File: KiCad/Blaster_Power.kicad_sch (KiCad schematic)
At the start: 17 parts, among them SW1 SW_SPST, U1 LT1172

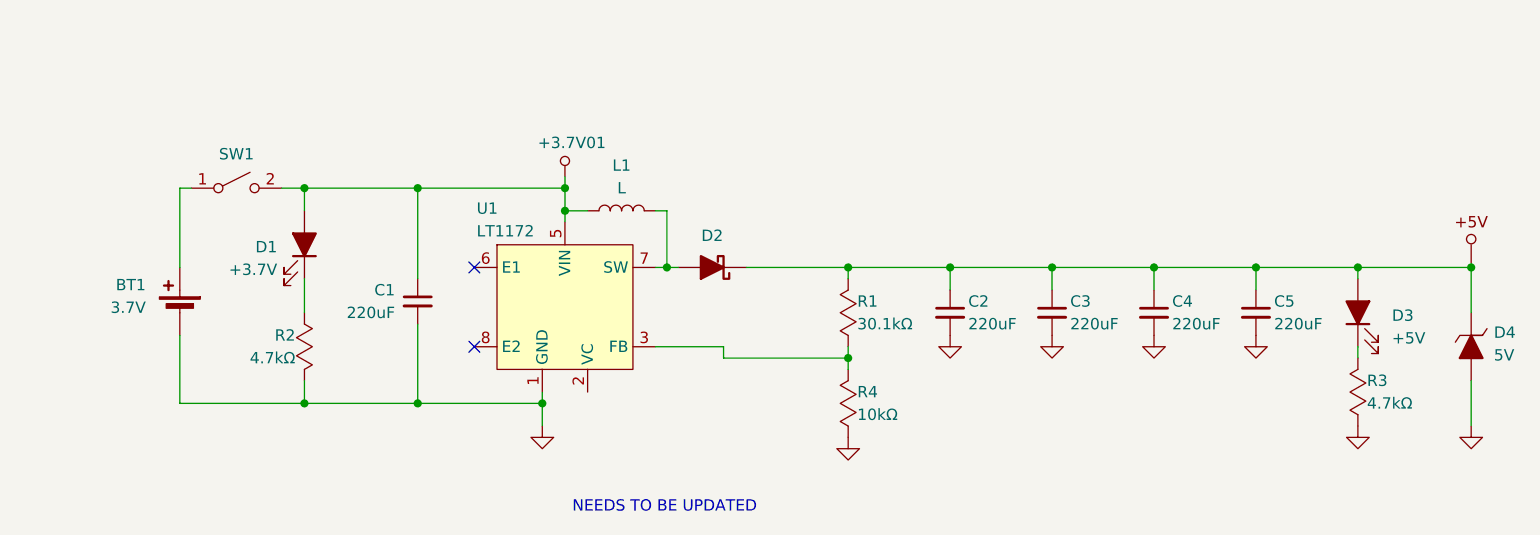
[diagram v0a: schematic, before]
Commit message: Updated blaster schematic
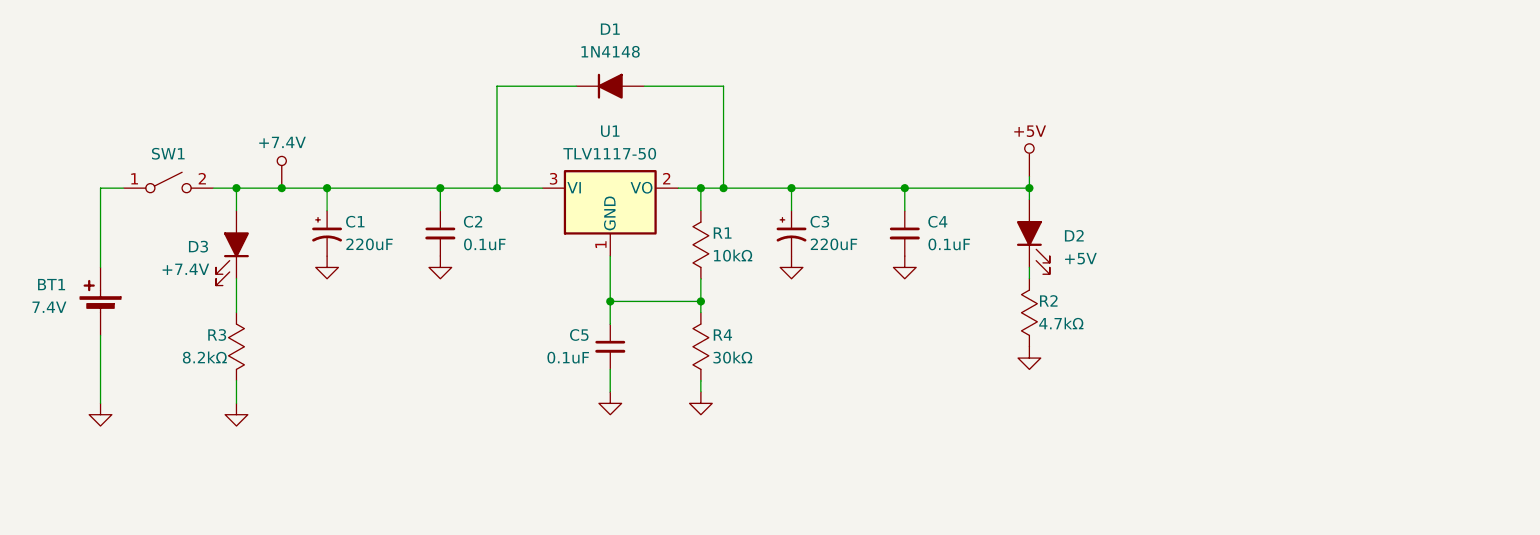
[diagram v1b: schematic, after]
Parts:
- removed C1, C3: 220uF, symbol Device:C_Small
- removed D2: D_Schottky_Filled, symbol Device:D_Schottky_Filled
- removed D4: 5V, symbol Libraries:D_Zener_Filled
- removed L1: L, symbol Device:L
- removed U1: LT1172, symbol Libraries:LT1172
- added C2: 0.1uF, symbol Device:C_Small
- added C3: 220uF, symbol Device:C_Polarized_Small_US
- added D1: 1N4148, symbol Device:D_Filled
- added U1: TLV1117-50, symbol Regulator_Linear:TLV1117-50
- BT1: value 3.7V -> 7.4V
- C1: renamed from C2; symbol Device:C_Small -> Device:C_Polarized_Small_US
- C4, C5: value 220uF -> 0.1uF
- D3: renamed from D1; value +3.7V -> +7.4V
- R1: value 30.1kΩ -> 10kΩ
- R3: renamed from R2; value 4.7kΩ -> 8.2kΩ
- R4: value 10kΩ -> 30kΩ
- renumbered D3 to D2, R3 to R2
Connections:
- net +5V: now also C3.1, D1.2 (A), U1.2 (VO); no longer C1.1, C5.1
- net GND: now also C2.2, C3.2
- net at D3.2 (A), SW1.2 (B): now also C1.1, C2.1, D1.1 (K), U1.3 (VI)
- net at R1.1, R4.2: now also C5.1, U1.1 (GND)
- no-connect marks 2 -> 0
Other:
- note removed: "NEEDS TO BE UPDATED"
- moved on the sheet: BT1, D2, D3, R2, R3, SW1

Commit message: Finalized schematics
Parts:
- removed C5: 0.1uF, symbol Device:C_Small
- removed R1: 10kΩ, symbol Libraries:R_Custom
- removed R4: 30kΩ, symbol Libraries:R_Custom
- added J2: Inputs Test Points, Connector_PinHeader_2.54mm:PinHeader_1x05_P2.54mm_Vertical, symbol Libraries:Header_1x5
- added J3: Power & Output Test Points, Connector_PinHeader_2.54mm:PinHeader_1x04_P2.54mm_Vertical, symbol Libraries:Header_1x4
- BT1: footprint (none) -> AlexWheelockFootprintLibrary:Project_Battery_Connector
- C1, C3: footprint (none) -> AlexWheelockFootprintLibrary:Project_16V_220uF_Capacitor
- C2, C4: footprint (none) -> Capacitor_SMD:C_0805_2012Metric_Pad1.18x1.45mm_HandSolder
- D1: footprint (none) -> Diode_SMD:D_0805_2012Metric_Pad1.15x1.40mm_HandSolder
- D2, D3: footprint (none) -> LED_SMD:LED_0805_2012Metric_Pad1.15x1.40mm_HandSolder
- R2, R3: footprint (none) -> Resistor_SMD:R_0805_2012Metric_Pad1.20x1.40mm_HandSolder
- SW1: value SW_SPST -> Power; footprint (none) -> AlexWheelockFootprintLibrary:Project_Locking_Output_Header
- U1: footprint (none) -> Package_TO_SOT_SMD:SOT-223-3_TabPin2
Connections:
- net +5V: now also J3.2
- net GND: now also U1.1 (GND)
- new net +7.4V: J3.1
- new net Burst: J2.4
- new net Fire: J2.1
- new net Frequency Select: J2.2
- new net Full-Auto: J2.3
- new net Laser/PWM: J3.3
- new net Semi-Auto: J2.5
- new net Solenoid: J3.4
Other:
- moved on the sheet: BT1

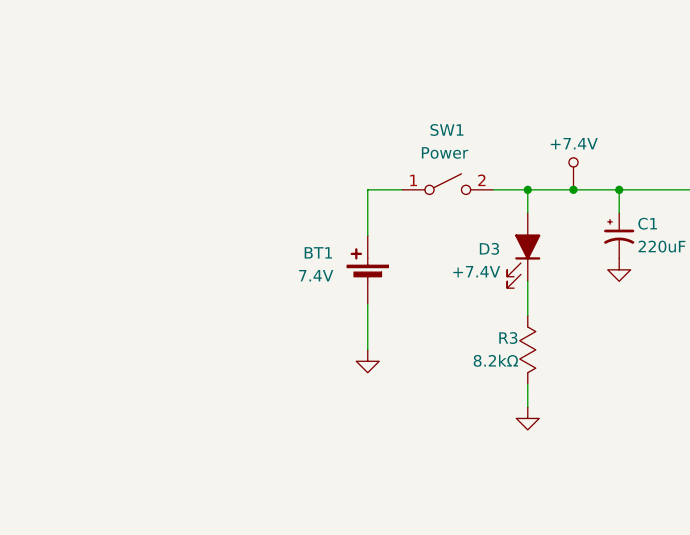
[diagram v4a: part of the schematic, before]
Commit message: recovered some lost parts of the schematic, still needs a bit of work to get back
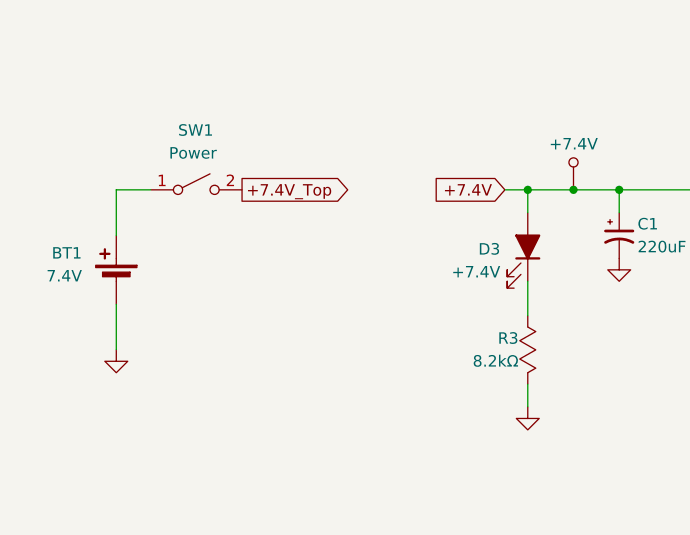
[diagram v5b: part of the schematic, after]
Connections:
- net +7.4V: now also C1.1, C2.1, D1.1 (K), D3.2 (A), U1.3 (VI)
- new net +7.4V_Top: SW1.2 (B)
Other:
- moved on the sheet: BT1, SW1
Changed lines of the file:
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@@
+	(wire
+		(pts
+			(xy 95.25 82.55) (xy 97.79 82.55)
+		)
+		(stroke
+			(width 0)
+			(type default)
+		)
+	)
 	(wire
 		(pts
@@
 	(wire
 		(pts
-			(xy 80.01 82.55) (xy 83.82 82.55)
+			(xy 52.07 82.55) (xy 55.88 82.55)
 		)
 		(stroke
@@
 	(wire
 		(pts
-			(xy 80.01 100.33) (xy 80.01 95.25)
+			(xy 52.07 100.33) (xy 52.07 95.25)
 		)
 		(stroke
@@
 	(wire
 		(pts
-			(xy 93.98 82.55) (xy 97.79 82.55)
-		)
-		(stroke
-			(width 0)
-			(type default)
-		)
-	)
-	(wire
-		(pts
 			(xy 82.55 172.72) (xy 85.09 172.72)
 		)
@@
 	(wire
 		(pts
-			(xy 80.01 87.63) (xy 80.01 82.55)
+			(xy 52.07 87.63) (xy 52.07 82.55)
 		)
 		(stroke
@@
 			(width 0)
 			(type default)
+		)
+	)
+	(global_label "+7.4V_Top"
+		(shape output)
+		(at 66.04 82.55 0)
+		(fields_autoplaced yes)
+		(effects
+			(font
+				(size 1.27 1.27)
+			)
+			(justify left)
+		)
+		(property "Intersheetrefs" "${INTERSHEET_REFS}"
+			(at 78.9432 82.55 0)
+			(effects
+				(font
+					(size 1.27 1.27)
+				)
+				(justify left)
+				(hide yes)
+			)
 		)
 	)
@@
 		)
 	)
+	(global_label "+7.4V"
+		(shape input)
+		(at 95.25 82.55 180)
+		(fields_autoplaced yes)
+		(effects
+			(font
+				(size 1.27 1.27)
+			)
+			(justify right)
+		)
+		(property "Intersheetrefs" "${INTERSHEET_REFS}"
+			(at 86.58 82.55 0)
+			(effects
+				(font
+					(size 1.27 1.27)
+				)
+				(justify right)
+				(hide yes)
+			)
+		)
+	)
 	(symbol
 		(lib_id "Switch:SW_SPST")
-		(at 88.9 82.55 0)
+		(at 60.96 82.55 0)
 		(unit 1)
 		(exclude_from_sim no)
@@
 		(dnp no)
 		(property "Reference" "SW1"
-			(at 86.868 75.946 0)
+			(at 58.928 75.946 0)
 			(effects
 				(font
@@
 		)
 		(property "Value" "Power"
-			(at 85.852 78.486 0)
+			(at 57.912 78.486 0)
 			(effects
 				(font
@@
 		)
 		(property "Footprint" "AlexWheelockFootprintLibrary:Project_Locking_Output_Header"
-			(at 88.9 82.55 0)
+			(at 60.96 82.55 0)
 			(effects
 				(font
@@
 		)
 		(property "Datasheet" "~"
-			(at 88.9 82.55 0)
+			(at 60.96 82.55 0)
 			(effects
 				(font
@@
 		)
 		(property "Description" "Single Pole Single Throw (SPST) switch"
-			(at 88.9 82.55 0)
+			(at 60.96 82.55 0)
 			(effects
 				(font
@@
 	(symbol
 		(lib_id "Device:Battery_Cell")
-		(at 80.01 92.71 0)
+		(at 52.07 92.71 0)
 		(mirror y)
 		(unit 1)
@@
 		(dnp no)
 		(property "Reference" "BT1"
-			(at 76.2 89.5984 0)
+			(at 48.26 89.5984 0)
 			(effects
 				(font
@@
 		)
 		(property "Value" "7.4V"
-			(at 76.2 92.1384 0)
+			(at 48.26 92.1384 0)
 			(effects
 				(font
@@
 		)
 		(property "Footprint" "AlexWheelockFootprintLibrary:Project_Battery_Connector"
-			(at 80.01 91.186 90)
+			(at 52.07 91.186 90)
 			(effects
 				(font
@@
 		)
 		(property "Datasheet" "~"
-			(at 80.01 91.186 90)
+			(at 52.07 91.186 90)
 			(effects
 				(font
@@
 		)
 		(property "Description" "Single-cell battery"
-			(at 80.01 92.71 0)
+			(at 52.07 92.71 0)
 			(effects
 				(font
@@
 	(symbol
 		(lib_id "power:GND")
-		(at 80.01 100.33 0)
+		(at 52.07 100.33 0)
 		(unit 1)
 		(exclude_from_sim no)
@@
 		(fields_autoplaced yes)
 		(property "Reference" "#PWR06"
-			(at 80.01 106.68 0)
+			(at 52.07 106.68 0)
 			(effects
 				(font
@@
 		)
 		(property "Value" "GND"
-			(at 80.01 105.41 0)
+			(at 52.07 105.41 0)
 			(effects
 				(font
@@
 		)
 		(property "Footprint" ""
-			(at 80.01 100.33 0)
+			(at 52.07 100.33 0)
 			(effects
 				(font
@@
 		)
 		(property "Datasheet" ""
-			(at 80.01 100.33 0)
+			(at 52.07 100.33 0)
 			(effects
 				(font
@@
 		)
 		(property "Description" "Power symbol creates a global label with name \"GND\" , ground"
-			(at 80.01 100.33 0)
-			(effects
-				(font
+			(at 52.07 100.33 0)
+			(effects
+				(font

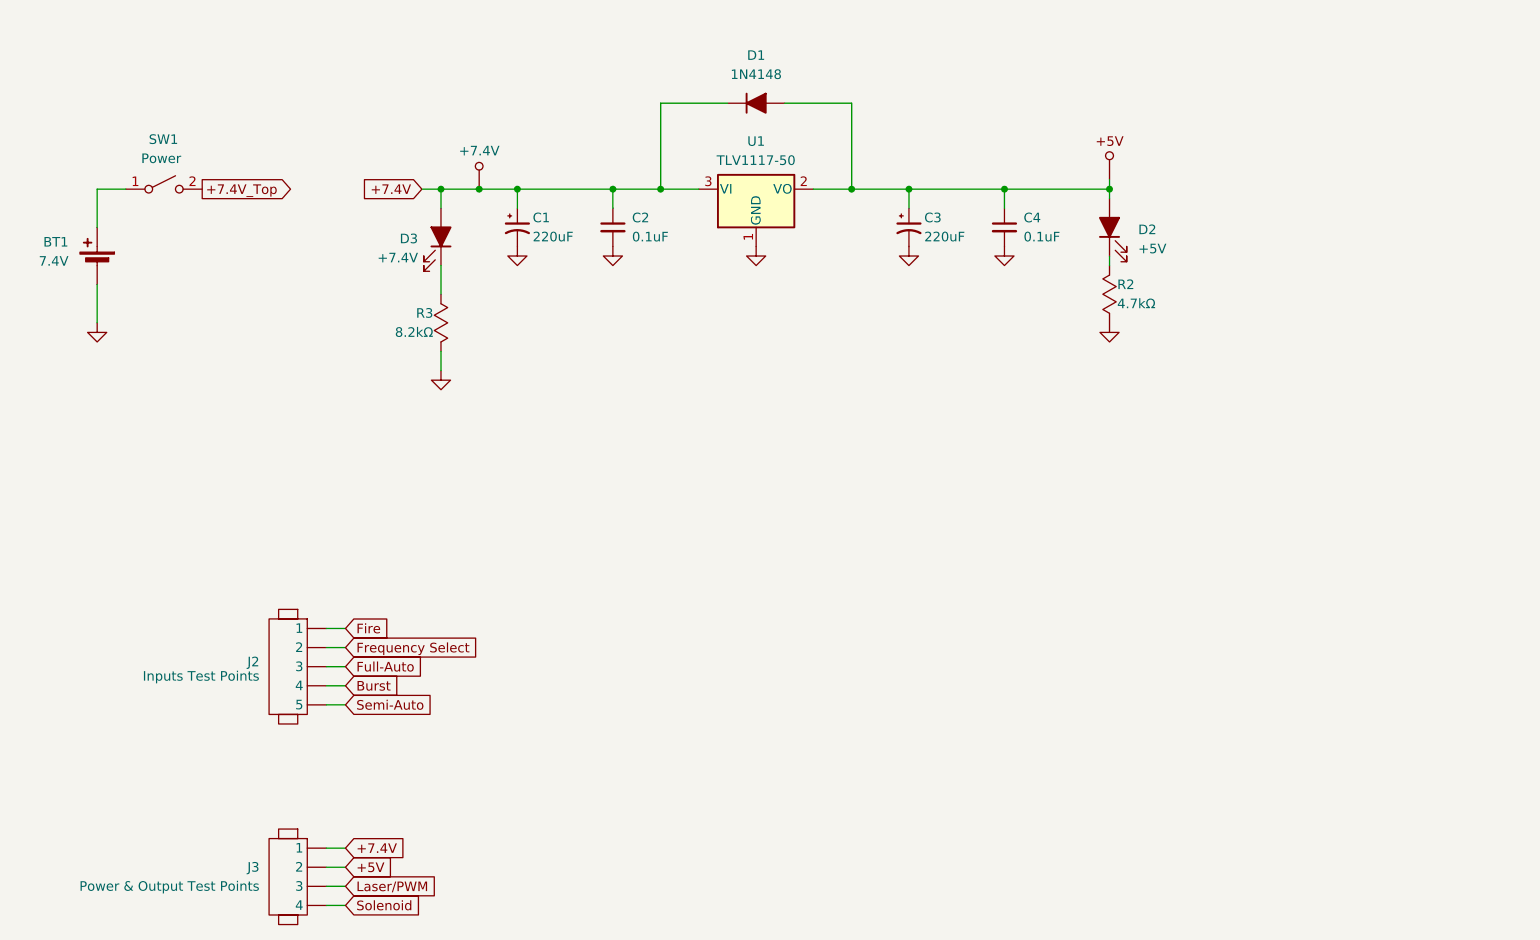
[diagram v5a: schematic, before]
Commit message: fixed the schematics, and got the new components added into the PCB, need to rerun a lot of traces.
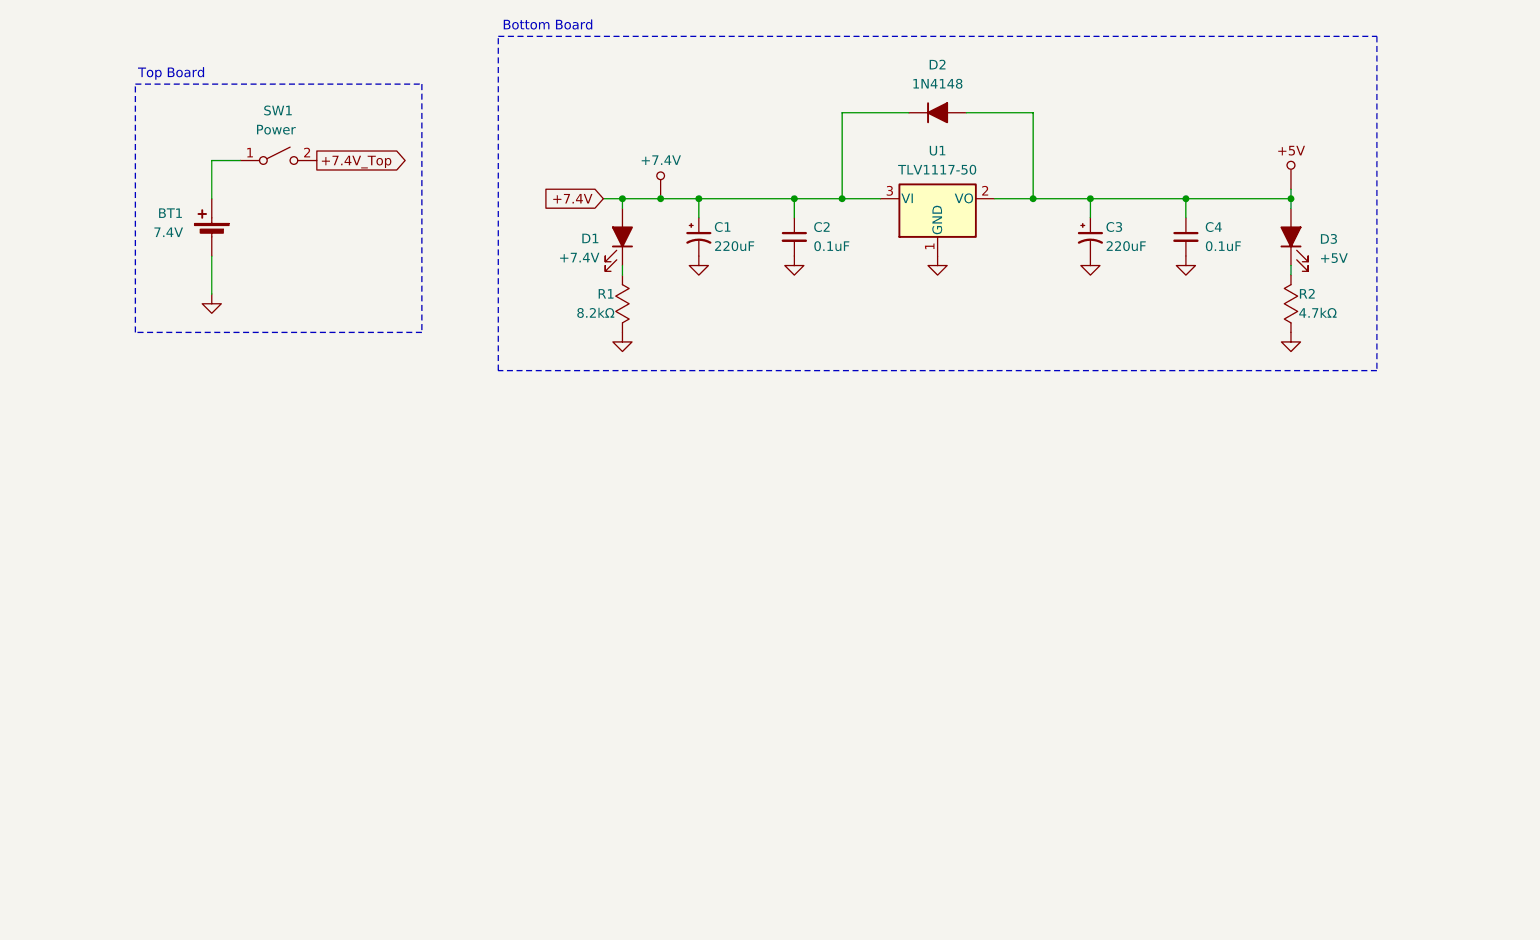
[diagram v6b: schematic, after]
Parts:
- removed J2: Inputs Test Points, Connector_PinHeader_2.54mm:PinHeader_1x05_P2.54mm_Vertical, symbol Libraries:Header_1x5
- removed J3: Power & Output Test Points, Connector_PinHeader_2.54mm:PinHeader_1x04_P2.54mm_Vertical, symbol Libraries:Header_1x4
- renumbered D3 to D1, D1 to D2, D2 to D3, R3 to R1
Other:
- note added: "Bottom Board"
- note added: "Top Board"
- moved on the sheet: BT1, C1, C2, C3, C4, D1, D2, D3, R1, R2, SW1, U1

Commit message: PCB nearly done for the blaster
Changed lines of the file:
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@@
+	)
+	(junction
+		(at 210.82 81.28)
+		(diameter 0)
+		(color 0 0 0 0)
 	)
 	(junction
@@
 	(wire
 		(pts
+			(xy 210.82 81.28) (xy 213.36 81.28)
+		)
+		(stroke
+			(width 0)
+			(type default)
+		)
+	)
+	(wire
+		(pts
 			(xy 151.13 83.82) (xy 156.21 83.82)
 		)
@@
 	(wire
 		(pts
-			(xy 210.82 83.82) (xy 210.82 82.55)
+			(xy 210.82 83.82) (xy 210.82 81.28)
 		)
 		(stroke
@@
 		(pts
 			(xy 171.45 83.82) (xy 176.53 83.82)
+		)
+		(stroke
+			(width 0)
+			(type default)
+		)
+	)
+	(wire
+		(pts
+			(xy 210.82 81.28) (xy 210.82 80.01)
 		)
 		(stroke
@@
 		)
 	)
+	(global_label "+5V"
+		(shape output)
+		(at 213.36 81.28 0)
+		(fields_autoplaced yes)
+		(effects
+			(font
+				(size 1.27 1.27)
+			)
+			(justify left)
+		)
+		(property "Intersheetrefs" "${INTERSHEET_REFS}"
+			(at 220.2157 81.28 0)
+			(effects
+				(font
+					(size 1.27 1.27)
+				)
+				(justify left)
+				(hide yes)
+			)
+		)
+	)
 	(global_label "+7.4V"
 		(shape input)
@@
 	(symbol
 		(lib_id "Libraries:+5V")
-		(at 210.82 81.28 0)
+		(at 210.82 78.74 0)
 		(unit 1)
 		(exclude_from_sim no)
@@
 		(fields_autoplaced yes)
 		(property "Reference" "#+5V01"
-			(at 210.82 77.47 0)
+			(at 210.82 74.93 0)
 			(effects
 				(font
@@
 		)
 		(property "Value" "+5V"
-			(at 210.82 77.47 0)
+			(at 210.82 74.93 0)
 			(effects
 				(font
@@
 		)
 		(property "Footprint" ""
-			(at 210.82 77.47 0)
+			(at 210.82 74.93 0)
 			(effects
 				(font
@@
 		)
 		(property "Datasheet" ""
-			(at 210.82 77.47 0)
+			(at 210.82 74.93 0)
 			(effects
 				(font
@@
 		)
 		(property "Description" ""
-			(at 210.82 81.28 0)
-			(effects
-				(font
+			(at 210.82 78.74 0)
+			(effects
+				(font
